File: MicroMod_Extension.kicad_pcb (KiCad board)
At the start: 4 copper layers, 38.4 x 38.4 mm, 80 parts, among them J1 2199230-4, J10 Conn_01x02, J11 Screw_Terminal_01x04, J2 XKB_U262-16XN-4BVC11, J3 RSP-122811-01, J4 Screw_Terminal_01x04, J5 Conn_01x08, J6 Conn_01x08, J7 Conn_01x04, J8 Conn_01x04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

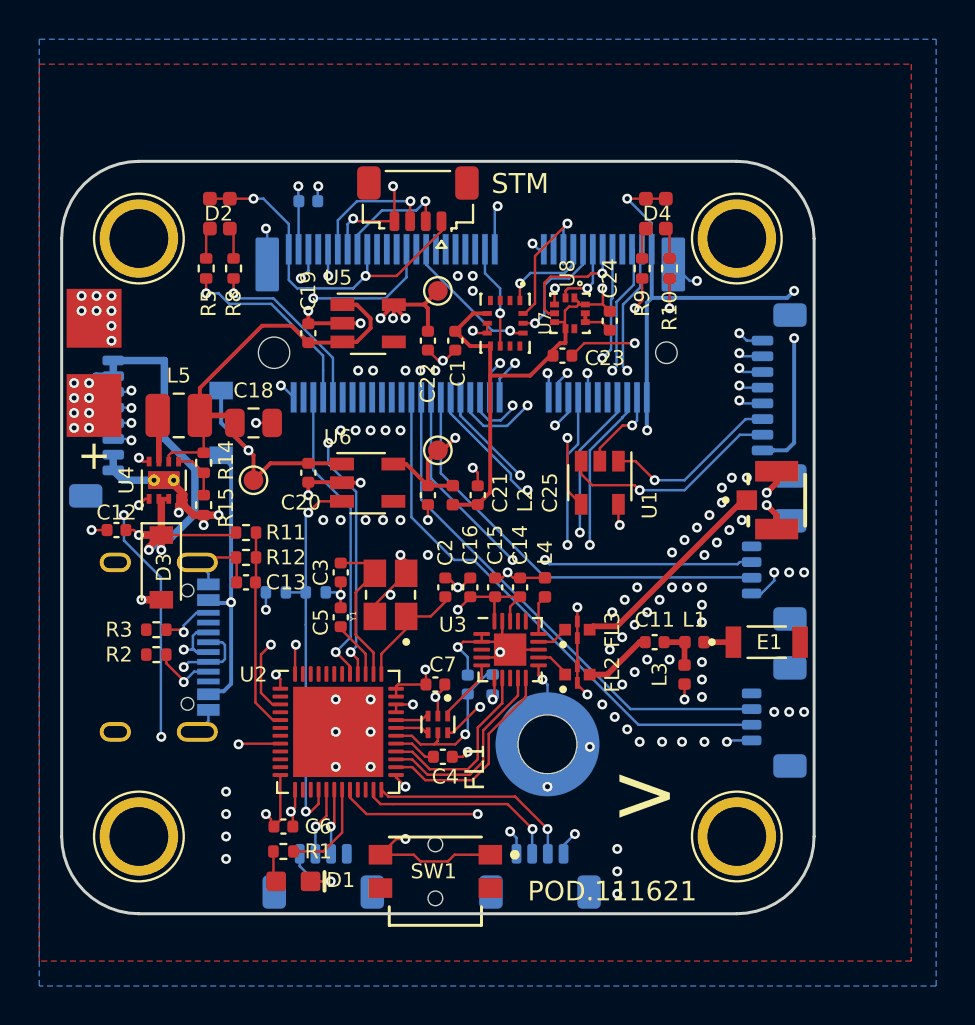
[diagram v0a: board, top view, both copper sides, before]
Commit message: change to iflight esc connection
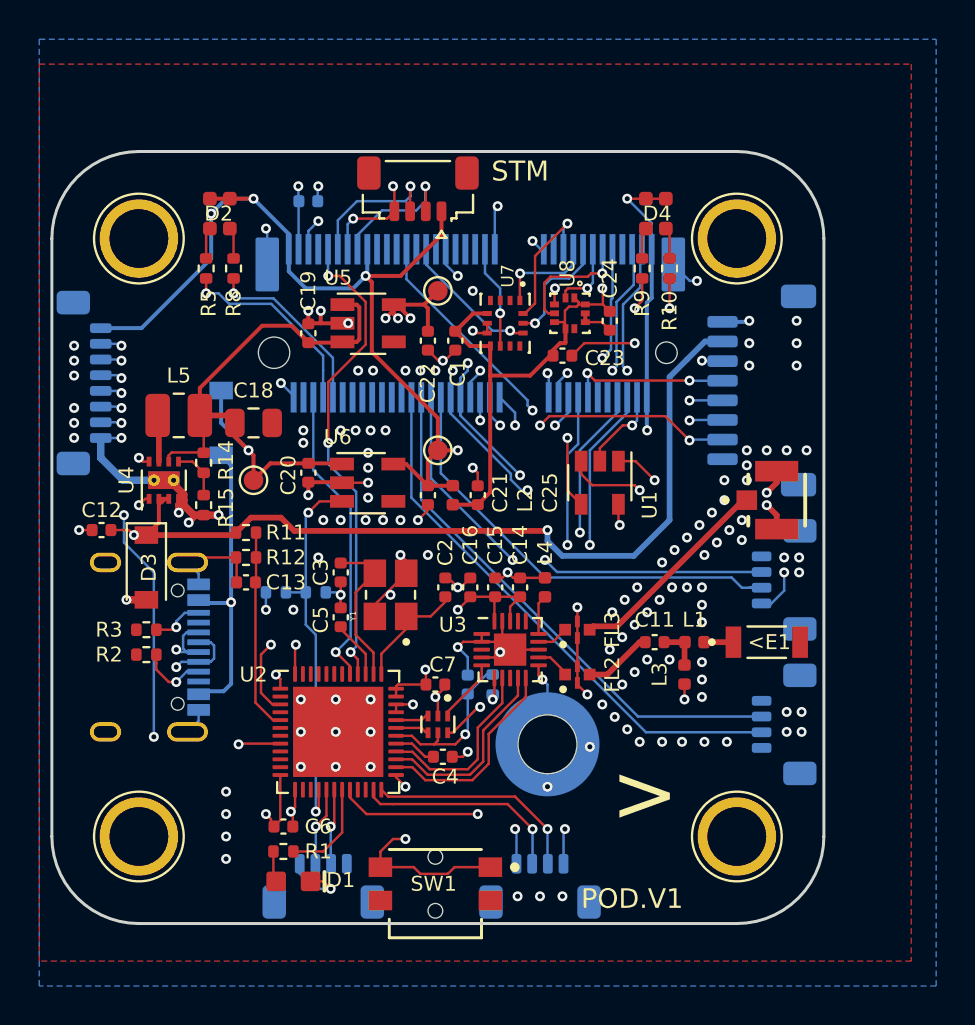
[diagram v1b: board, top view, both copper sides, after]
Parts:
- removed J10: Conn_01x02, MicroMod_Extension:BATTARY
- J5: footprint Connector_JST:JST_SUR_BM08B-SURS-TF_1x08-1MP_P0.80mm_Vertical -> Connector_JST:JST_SH_SM08B-SRSS-TB_1x08-1MP_P1.00mm_Horizontal
- moved J6 35.4 mm to (126.7, 55.6), turned to 270 degrees
- moved J5 33.9 mm to (161.3, 56.0)
- moved D3 0.76 mm to (129.9, 65.0)
- moved C12 0.76 mm to (127.6, 63.1)
- moved J8 0.72 mm to (162.4, 65.7)
- moved SW1 0.64 mm to (144.7, 81.2)
- moved J9 0.63 mm to (162.4, 73.0)
- moved R2 0.51 mm to (129.9, 69.5)
- moved R3 0.51 mm to (129.9, 68.2)
- moved J11 0.51 mm to (143.8, 45.7)
- moved J4 0.51 mm to (150.0, 81.3)
- moved J7 0.51 mm to (138.9, 81.3)
- moved J2 0.50 mm to (128.9, 69.1)
- renumbered E1 to <E1
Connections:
- J5 pad 1: BATT -> GND
- J5 pad 3: /MOTOR1 -> /MOTOR2
- J5 pad 4: /MOTOR2 -> /MOTOR1
- J5 pad 7: GND -> /C4
- J5 pad 8: GND -> Net-(J5-Pad8)
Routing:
- net /C4: track 0.00 -> 21.9 mm, vias 0 -> 3
- net /MOTOR1: track 26.0 -> 8.26 mm
- net /E_SCL: track 22.0 -> 38.0 mm, vias 2 -> 4
- net /E_SDA: track 24.4 -> 38.4 mm, vias 2 -> 4
- net /MOTOR3: track 14.3 -> 27.5 mm
- net /MOTOR2: track 26.3 -> 15.8 mm
- net BATT: track 35.9 -> 43.9 mm, vias 11 -> 2
- net /B4: track 16.4 -> 23.7 mm
- net /E_SPI_SCK: track 17.5 -> 22.5 mm
- net /E_SPI_MOSI: track 18.0 -> 22.8 mm
- net /E_SPI_MISO: track 16.7 -> 21.5 mm
- net /VCC: track 80.3 -> 75.8 mm, vias 8 -> 7
- net GND: track 108.0 -> 110.0 mm, vias 136 -> 155
- net /STM_NRST: track 22.5 -> 24.4 mm
- net /OTG_FS_D+: track 42.3 -> 43.8 mm
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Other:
- board size 38.4 x 38.4 mm -> 39.4 x 39.4 mm
- board text added: "POD.V1"
- board text removed: "+"
- board text removed: "POD.111621"

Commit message: add i2c connector
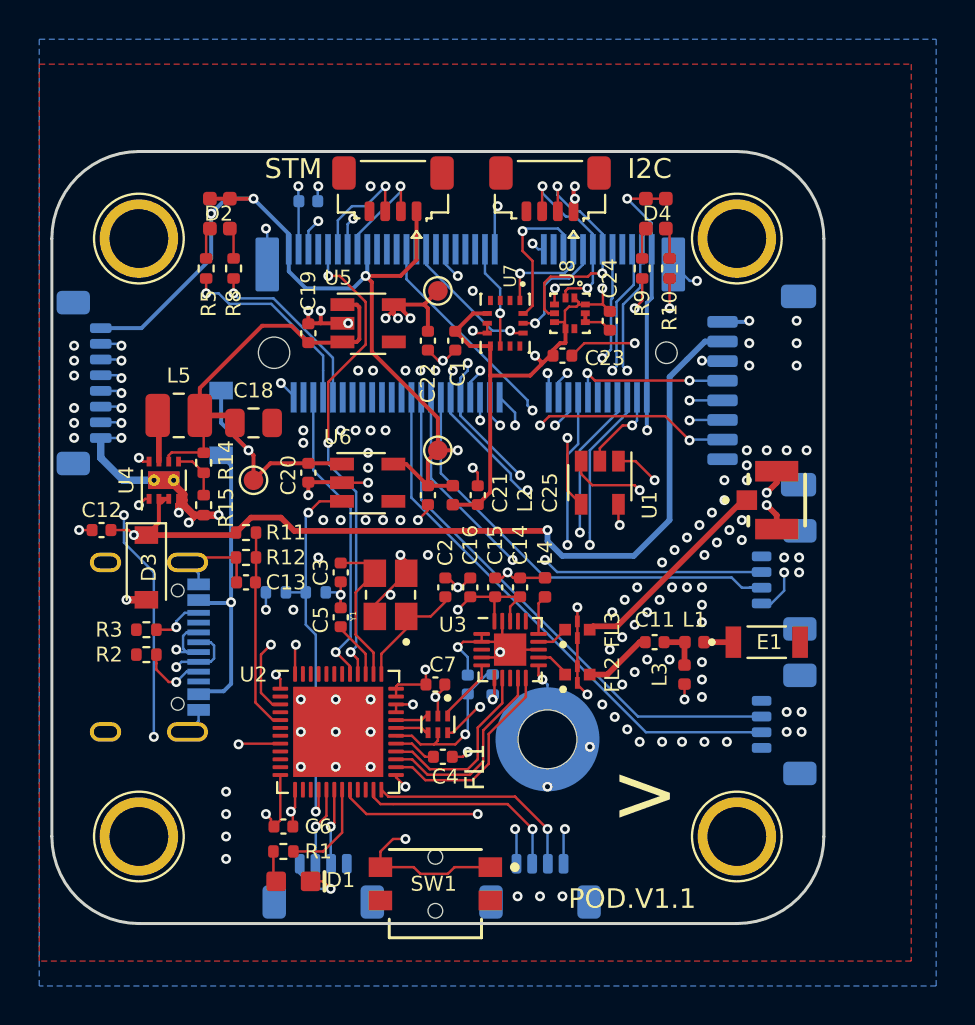
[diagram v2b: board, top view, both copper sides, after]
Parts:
- added J10: Conn_01x04, Connector_JST:JST_SUR_SM04B-SURS-TF_1x04-1MP_P0.80mm_Horizontal, F.Cu at (150.5, 45.7)
- moved J11 1.27 mm to (142.5, 45.7)
- moved TP8 0.25 mm to (150.4, 73.8)
- renumbered <E1 to E1
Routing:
- net /VCCI: track 24.6 -> 36.0 mm, vias 1 -> 4
- net /IMU_SCL: track 3.64 -> 9.48 mm, vias 1 -> 2
- net /IMU_SDA: track 6.39 -> 12.2 mm, vias 1 -> 2
- net GND: track 110.0 -> 106.4 mm
- net /STM_SWIO: track 7.48 -> 5.91 mm
- net /STM_SWCLK: track 6.95 -> 5.41 mm
- net /SPI2_MOSI: track 6.96 -> 7.69 mm
- net /VCC: track 75.8 -> 75.3 mm
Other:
- board text added: "I2C"
- board text added: "POD.V1.1"
- board text removed: "POD.V1"
